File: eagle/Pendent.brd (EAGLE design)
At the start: 47.5 x 40.6 mm, 40 parts, among them Q1 CMA-4544PF-W, Q2 MPSA42, Q3 8/16/20MHz, U1 MAX9814TDFN14, U2 LF50ABDT-TR, U3 ATMEGA328

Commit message: Wire up Sleep Button
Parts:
- moved S2 51.6 mm to (44.2, 20.3), flipped to the bottom, turned to 270 degrees
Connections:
- net D10: now also R7.2
- net D9: no longer R7.2
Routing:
- net D3: track 2.42 -> 20.7 mm
- net D10: track 0.00 -> 7.73 mm
- net D9: track 8.74 -> 16.0 mm, vias 0 -> 1
- net VIN: track 52.2 -> 48.1 mm
- net D5: track 10.9 -> 12.4 mm
- net VCC: track 166.1 -> 167.3 mm
- net GND: track 5.69 -> 6.45 mm

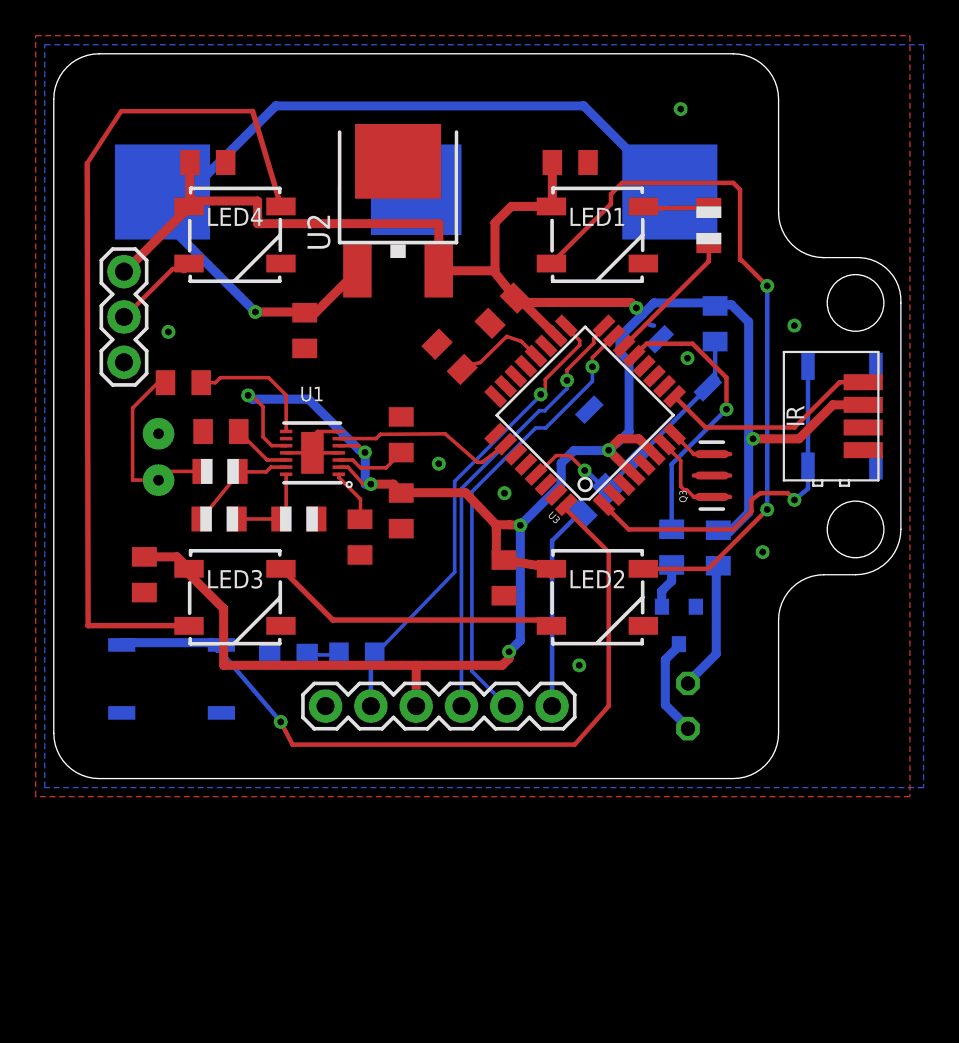
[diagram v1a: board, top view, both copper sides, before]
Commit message: Add Bigger Tempo Button to board
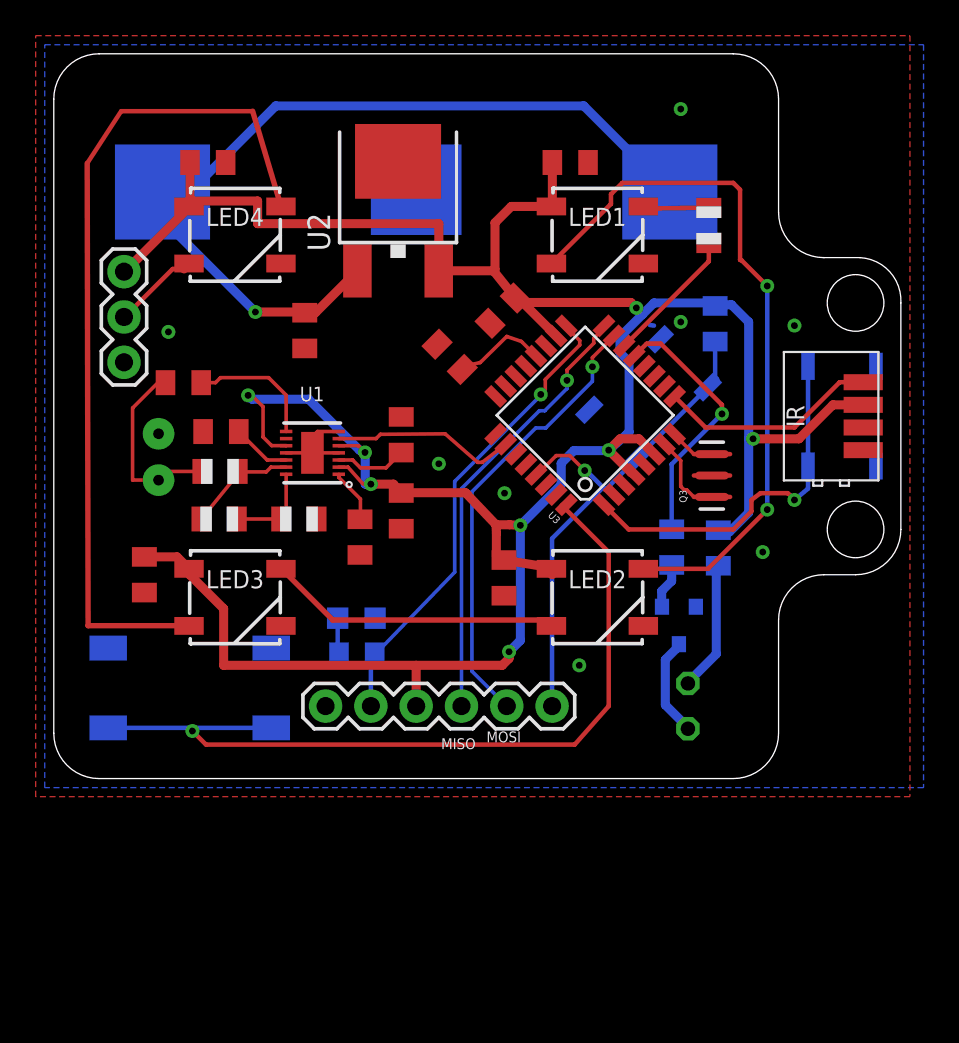
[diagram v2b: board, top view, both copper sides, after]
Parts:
- removed C14: 0.1uF, adafruit:C0805K
- S1: device SparkFun-Electromechanical:TACTILE-SWITCH-SMD -> bg_eagle_lib:2-1437565-7
- moved D3 4.32 mm to (17.0, 8.99), turned to 90 degrees
- moved S1 1.14 mm to (7.62, 5.08)
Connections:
- removed net RST: C14.2, JP10.1
- net D2: now also S1.P1, S1.P2; no longer S1.1, S1.2
- net GND: now also S1.P3, S1.P4; no longer S1.3, S1.4
- net RESET: now also JP10.1; no longer C14.1
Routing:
- net RESET: track 16.1 -> 29.5 mm
- net RST: track 11.6 -> 0.00 mm
- net D2: track 43.9 -> 46.4 mm
- net D9: track 16.0 -> 14.8 mm
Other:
- board text added: "MISO"
- board text added: "MOSI"
- board text added: "REV A"
- board text added: "SCK"
